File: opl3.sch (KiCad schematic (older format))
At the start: 20 parts

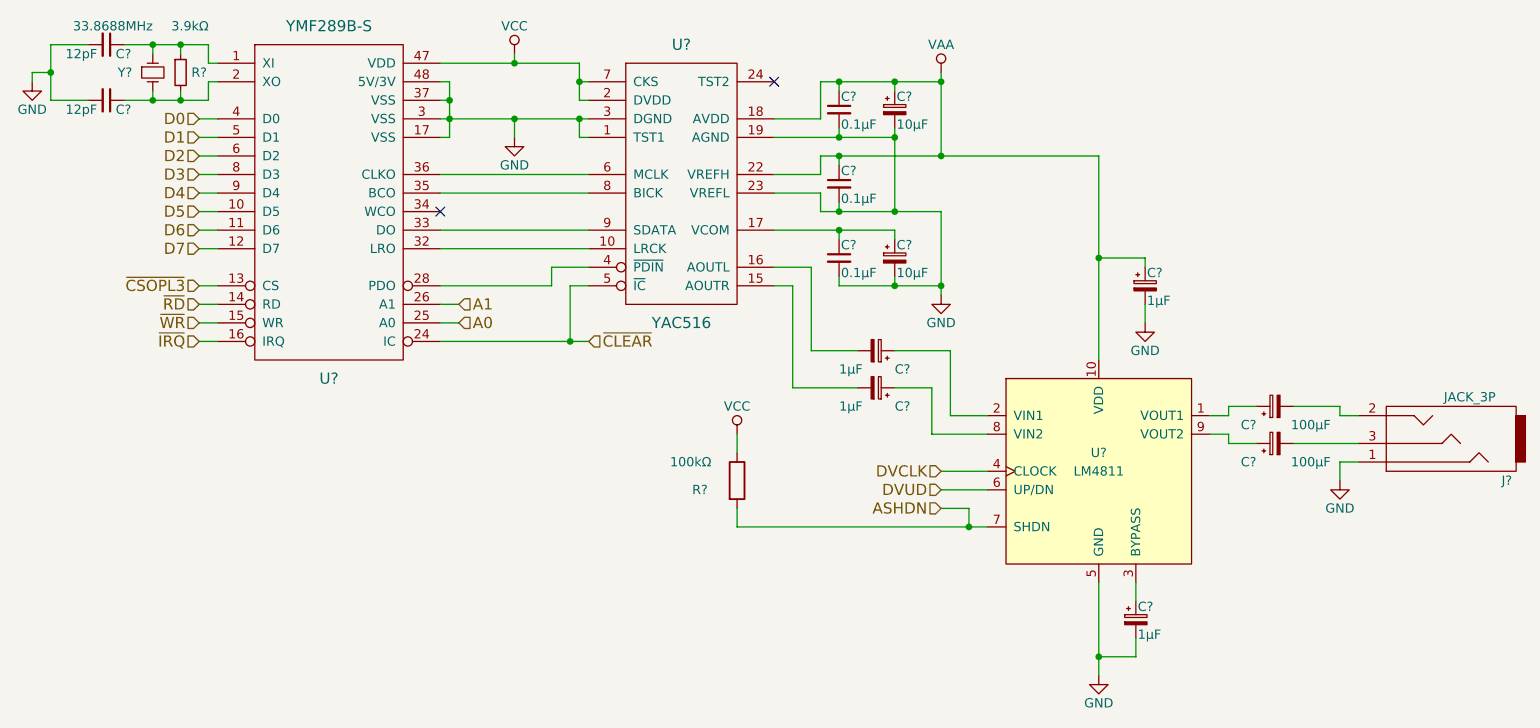
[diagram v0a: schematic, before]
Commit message: add more circuitry to schematic
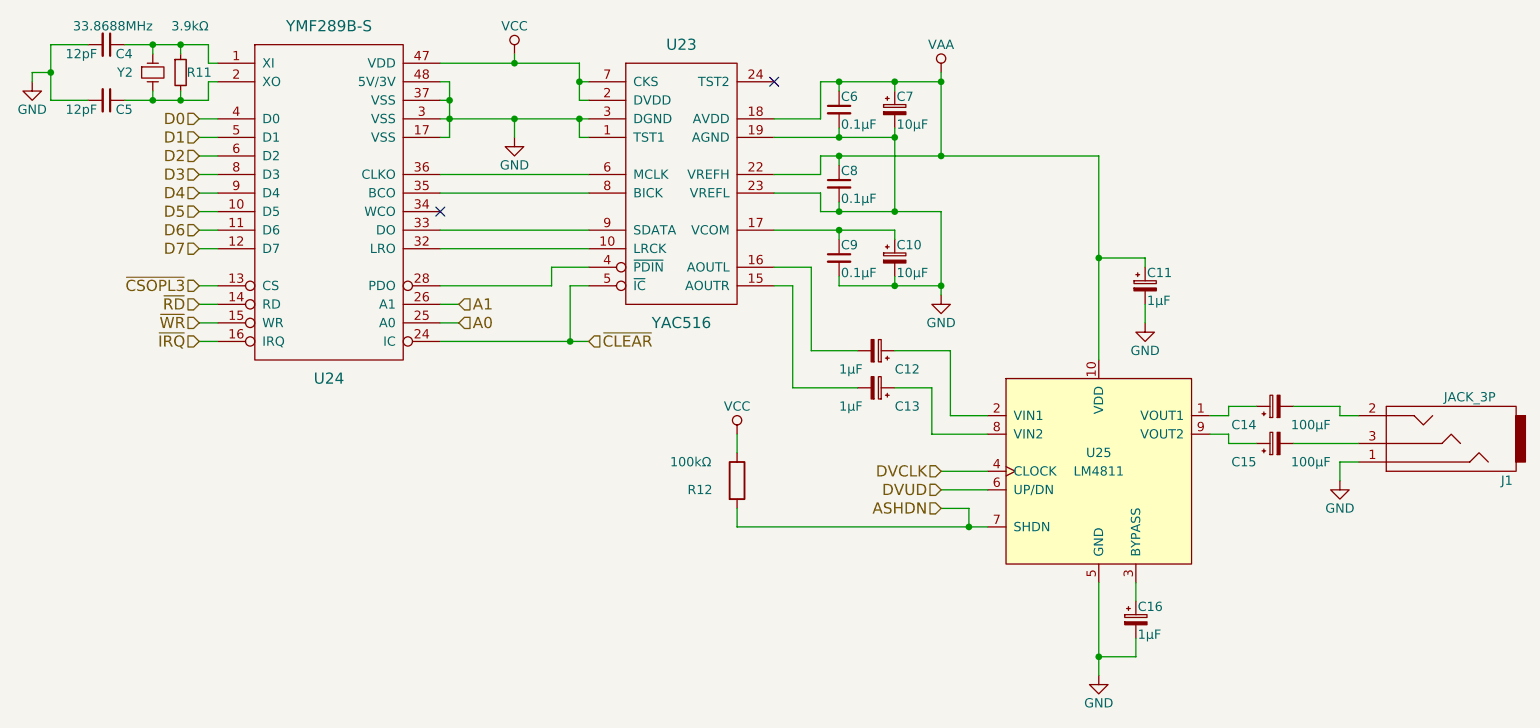
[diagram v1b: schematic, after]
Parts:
- gave numbers to parts that had none: 20
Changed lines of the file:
@@
 $EndDescr
 $Comp
-L YMF289B-S U?
+L YMF289B-S U24
 U 1 1 575AF34B
 P 3850 2850
-F 0 "U?" H 3850 1900 60  0000 C CNN
+F 0 "U24" H 3850 1900 60  0000 C CNN
 F 1 "YMF289B-S" H 3850 3800 60  0000 C CNN
 F 2 "" H 3850 2750 60  0000 C CNN
@@
 $EndComp
 $Comp
-L Crystal_Small Y?
+L Crystal_Small Y2
 U 1 1 575AF6C5
 P 2900 2150
-F 0 "Y?" V 2900 2000 50  0000 C CNN
+F 0 "Y2" V 2900 2000 50  0000 C CNN
 F 1 "33.8688MHz" V 2650 2150 50  0000 R CNN
 F 2 "" H 2900 2150 50  0000 C CNN
@@
 $EndComp
 $Comp
-L R_Small R?
+L R_Small R11
 U 1 1 575AF766
 P 3050 2150
-F 0 "R?" H 3150 2150 50  0000 C CNN
+F 0 "R11" H 3150 2150 50  0000 C CNN
 F 1 "3.9kΩ" H 3000 2400 50  0000 L CNN
 F 2 "" H 3050 2150 50  0000 C CNN
@@
 $EndComp
 $Comp
-L C_Small C?
+L C_Small C5
 U 1 1 575AF9D0
 P 2650 2300
-F 0 "C?" V 2700 2350 50  0000 L CNN
+F 0 "C5" V 2700 2350 50  0000 L CNN
 F 1 "12pF" V 2700 2250 50  0000 R CNN
 F 2 "" H 2650 2300 50  0000 C CNN
@@
 $EndComp
 $Comp
-L C_Small C?
+L C_Small C4
 U 1 1 575AFDA9
 P 2650 2000
-F 0 "C?" V 2700 2050 50  0000 L CNN
+F 0 "C4" V 2700 2050 50  0000 L CNN
 F 1 "12pF" V 2700 1950 50  0000 R CNN
 F 2 "" H 2650 2000 50  0000 C CNN
@@
 $EndComp
 $Comp
-L GND #PWR?
+L GND #PWR19
 U 1 1 575AFF49
 P 2250 2200
-F 0 "#PWR?" H 2250 1950 50  0001 C CNN
+F 0 "#PWR19" H 2250 1950 50  0001 C CNN
 F 1 "GND" H 2250 2050 50  0000 C CNN
 F 2 "" H 2250 2200 50  0000 C CNN
@@
 A1
 $Comp
-L GND #PWR?
+L GND #PWR20
 U 1 1 575B62A5
 P 4850 2500
-F 0 "#PWR?" H 4850 2250 50  0001 C CNN
+F 0 "#PWR20" H 4850 2250 50  0001 C CNN
 F 1 "GND" H 4850 2350 50  0000 C CNN
 F 2 "" H 4850 2500 50  0000 C CNN
@@
 $EndComp
 $Comp
-L VCC #PWR?
+L VCC #PWR17
 U 1 1 575B62C3
 P 4850 2050
-F 0 "#PWR?" H 4850 1900 50  0001 C CNN
+F 0 "#PWR17" H 4850 1900 50  0001 C CNN
 F 1 "VCC" H 4850 2200 50  0000 C CNN
 F 2 "" H 4850 2050 50  0000 C CNN
@@
 ~CLEAR
 $Comp
-L YAC516 U?
+L YAC516 U23
 U 1 1 575E7517
 P 5750 2750
-F 0 "U?" H 5750 3500 60  0000 C CNN
+F 0 "U23" H 5750 3500 60  0000 C CNN
 F 1 "YAC516" H 5750 2000 60  0000 C CNN
 F 2 "" H 5750 3400 60  0000 C CNN
@@
 Connection ~ 6900 2200
 $Comp
-L CP_Small C?
+L CP_Small C7
 U 1 1 575EB371
 P 6900 2350
-F 0 "C?" H 6910 2420 50  0000 L CNN
+F 0 "C7" H 6910 2420 50  0000 L CNN
 F 1 "10μF" H 6910 2270 50  0000 L CNN
 F 2 "" H 6900 2350 50  0000 C CNN
@@
 	6250 3000 6900 3000
 $Comp
-L CP_Small C?
+L CP_Small C10
 U 1 1 575EA4F0
 P 6900 3150
-F 0 "C?" H 6910 3220 50  0000 L CNN
+F 0 "C10" H 6910 3220 50  0000 L CNN
 F 1 "10μF" H 6910 3070 50  0000 L CNN
 F 2 "" H 6900 3150 50  0000 C CNN
@@
 $EndComp
 $Comp
-L C_Small C?
+L C_Small C9
 U 1 1 575EA4A0
 P 6600 3150
-F 0 "C?" H 6610 3220 50  0000 L CNN
+F 0 "C9" H 6610 3220 50  0000 L CNN
 F 1 "0.1μF" H 6610 3070 50  0000 L CNN
 F 2 "" H 6600 3150 50  0000 C CNN
@@
 	6500 2400 6250 2400
 $Comp
-L VAA #PWR?
+L VAA #PWR18
 U 1 1 575E9D68
 P 7150 2150
-F 0 "#PWR?" H 7150 2000 50  0001 C CNN
+F 0 "#PWR18" H 7150 2000 50  0001 C CNN
 F 1 "VAA" H 7150 2300 50  0000 C CNN
 F 2 "" H 7150 2150 50  0000 C CNN
@@
 Connection ~ 6600 2600
 $Comp
-L GND #PWR?
+L GND #PWR21
 U 1 1 575E9C3E
 P 7150 3350
-F 0 "#PWR?" H 7150 3100 50  0001 C CNN
+F 0 "#PWR21" H 7150 3100 50  0001 C CNN
 F 1 "GND" H 7150 3200 50  0000 C CNN
 F 2 "" H 7150 3350 50  0000 C CNN
@@
 	6600 2250 6600 2200
 $Comp
-L C_Small C?
+L C_Small C6
 U 1 1 575E8DBB
 P 6600 2350
-F 0 "C?" H 6610 2420 50  0000 L CNN
+F 0 "C6" H 6610 2420 50  0000 L CNN
 F 1 "0.1μF" H 6610 2270 50  0000 L CNN
 F 2 "" H 6600 2350 50  0000 C CNN
@@
 $EndComp
 $Comp
-L C_Small C?
+L C_Small C8
 U 1 1 575E8D86
 P 6600 2750
-F 0 "C?" H 6610 2820 50  0000 L CNN
+F 0 "C8" H 6610 2820 50  0000 L CNN
 F 1 "0.1μF" H 6610 2670 50  0000 L CNN
 F 2 "" H 6600 2750 50  0000 C CNN
@@
 $EndComp
 $Comp
-L LM4811 U?
+L LM4811 U25
 U 1 1 57652DA8
 P 8000 4300
-F 0 "U?" H 8000 4400 50  0000 C CNN
+F 0 "U25" H 8000 4400 50  0000 C CNN
 F 1 "LM4811" H 8000 4300 50  0000 C CNN
 F 2 "" H 8000 4200 50  0000 C CIN
@@
 	6250 3300 6350 3300
 $Comp
-L GND #PWR?
+L GND #PWR25
 U 1 1 57655F46
 P 8000 5400
-F 0 "#PWR?" H 8000 5150 50  0001 C CNN
+F 0 "#PWR25" H 8000 5150 50  0001 C CNN
 F 1 "GND" H 8000 5250 50  0000 C CNN
 F 2 "" H 8000 5400 50  0000 C CNN
@@
 	8000 4900 8000 5400
 $Comp
-L CP_Small C?
+L CP_Small C16
 U 1 1 576560A8
 P 8200 5100
-F 0 "C?" H 8210 5170 50  0000 L CNN
+F 0 "C16" H 8210 5170 50  0000 L CNN
 F 1 "1μF" H 8210 5020 50  0000 L CNN
 F 2 "" H 8200 5100 50  0000 C CNN
@@
 Connection ~ 7150 2600
 $Comp
-L CP_Small C?
+L CP_Small C15
 U 1 1 576517D1
 P 8950 4150
-F 0 "C?" V 8850 4250 50  0000 L CNN
+F 0 "C15" V 8850 4250 50  0000 L CNN
 F 1 "100μF" V 8850 3850 50  0000 L CNN
 F 2 "" H 8950 4150 50  0000 C CNN
@@
 $EndComp
 $Comp
-L CP_Small C?
+L CP_Small C14
 U 1 1 57652739
 P 8950 3950
-F 0 "C?" V 8850 4050 50  0000 L CNN
+F 0 "C14" V 8850 4050 50  0000 L CNN
 F 1 "100μF" V 8850 3650 50  0000 L CNN
 F 2 "" H 8950 3950 50  0000 C CNN
@@
 $EndComp
 $Comp
-L JACK_3P J?
+L JACK_3P J1
 U 1 1 5765375D
 P 9850 4150
-F 0 "J?" H 9500 3950 50  0000 C CNN
+F 0 "J1" H 9500 3950 50  0000 C CNN
 F 1 "JACK_3P" H 9700 4400 50  0000 C CNN
 F 2 "" H 10050 3500 50  0000 C CNN
@@
 	9300 4250 9300 4350
 $Comp
-L GND #PWR?
+L GND #PWR24
 U 1 1 576548E0
 P 9300 4350
-F 0 "#PWR?" H 9300 4100 50  0001 C CNN
+F 0 "#PWR24" H 9300 4100 50  0001 C CNN
 F 1 "GND" H 9300 4200 50  0000 C CNN
 F 2 "" H 9300 4350 50  0000 C CNN
@@
 $EndComp
 $Comp
-L VCC #PWR?
+L VCC #PWR23
 U 1 1 57654CF4
 P 6050 4100
-F 0 "#PWR?" H 6050 3950 50  0001 C CNN
+F 0 "#PWR23" H 6050 3950 50  0001 C CNN
 F 1 "VCC" H 6050 4250 50  0000 C CNN
 F 2 "" H 6050 4100 50  0000 C CNN
@@
 $EndComp
 $Comp
-L R R?
+L R R12
 U 1 1 57654D28
 P 6050 4350
-F 0 "R?" H 5850 4300 50  0000 C CNN
+F 0 "R12" H 5850 4300 50  0000 C CNN
 F 1 "100kΩ" H 5800 4450 50  0000 C CNN
 F 2 "" V 5980 4350 50  0000 C CNN
@@
 	7400 4400 7150 4400
 $Comp
-L CP_Small C?
+L CP_Small C11
 U 1 1 57656420
 P 8250 3300
-F 0 "C?" H 8260 3370 50  0000 L CNN
+F 0 "C11" H 8260 3370 50  0000 L CNN
 F 1 "1μF" H 8260 3220 50  0000 L CNN
 F 2 "" H 8250 3300 50  0000 C CNN
@@
 $EndComp
 $Comp
-L GND #PWR?
+L GND #PWR22
 U 1 1 57656476
 P 8250 3500
-F 0 "#PWR?" H 8250 3250 50  0001 C CNN
+F 0 "#PWR22" H 8250 3250 50  0001 C CNN
 F 1 "GND" H 8250 3350 50  0000 C CNN
 F 2 "" H 8250 3500 50  0000 C CNN
@@
 Connection ~ 8000 3150
 $Comp
-L CP_Small C?
+L CP_Small C13
 U 1 1 57656A28
 P 6800 3850
-F 0 "C?" V 6700 3950 50  0000 L CNN
+F 0 "C13" V 6700 3950 50  0000 L CNN
 F 1 "1μF" V 6700 3650 50  0000 L CNN
 F 2 "" H 6800 3850 50  0000 C CNN
@@
 $EndComp
 $Comp
-L CP_Small C?
+L CP_Small C12
 U 1 1 57656A2E
 P 6800 3650
-F 0 "C?" V 6700 3750 50  0000 L CNN
+F 0 "C12" V 6700 3750 50  0000 L CNN
 F 1 "1μF" V 6700 3450 50  0000 L CNN
 F 2 "" H 6800 3650 50  0000 C CNN
